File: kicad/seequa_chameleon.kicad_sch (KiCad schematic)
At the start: 0 parts

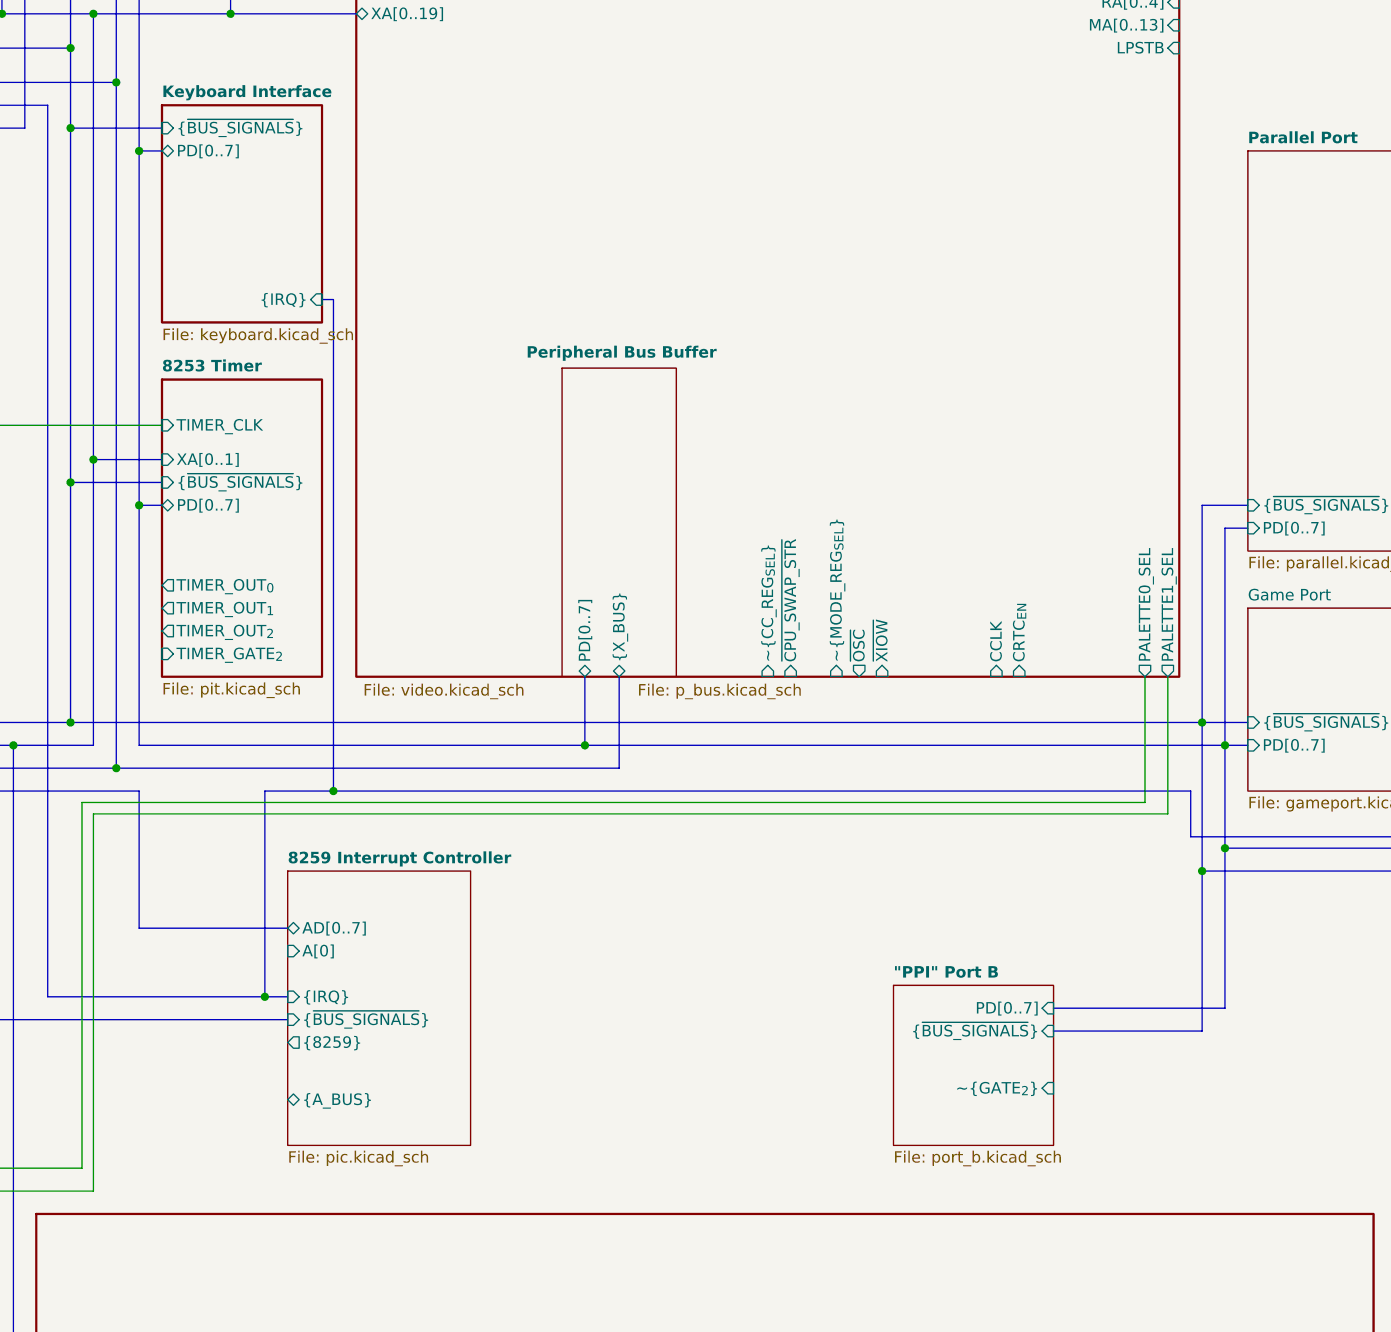
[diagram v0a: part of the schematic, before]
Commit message: Fixes to clocks,  keyboard controller stuff.
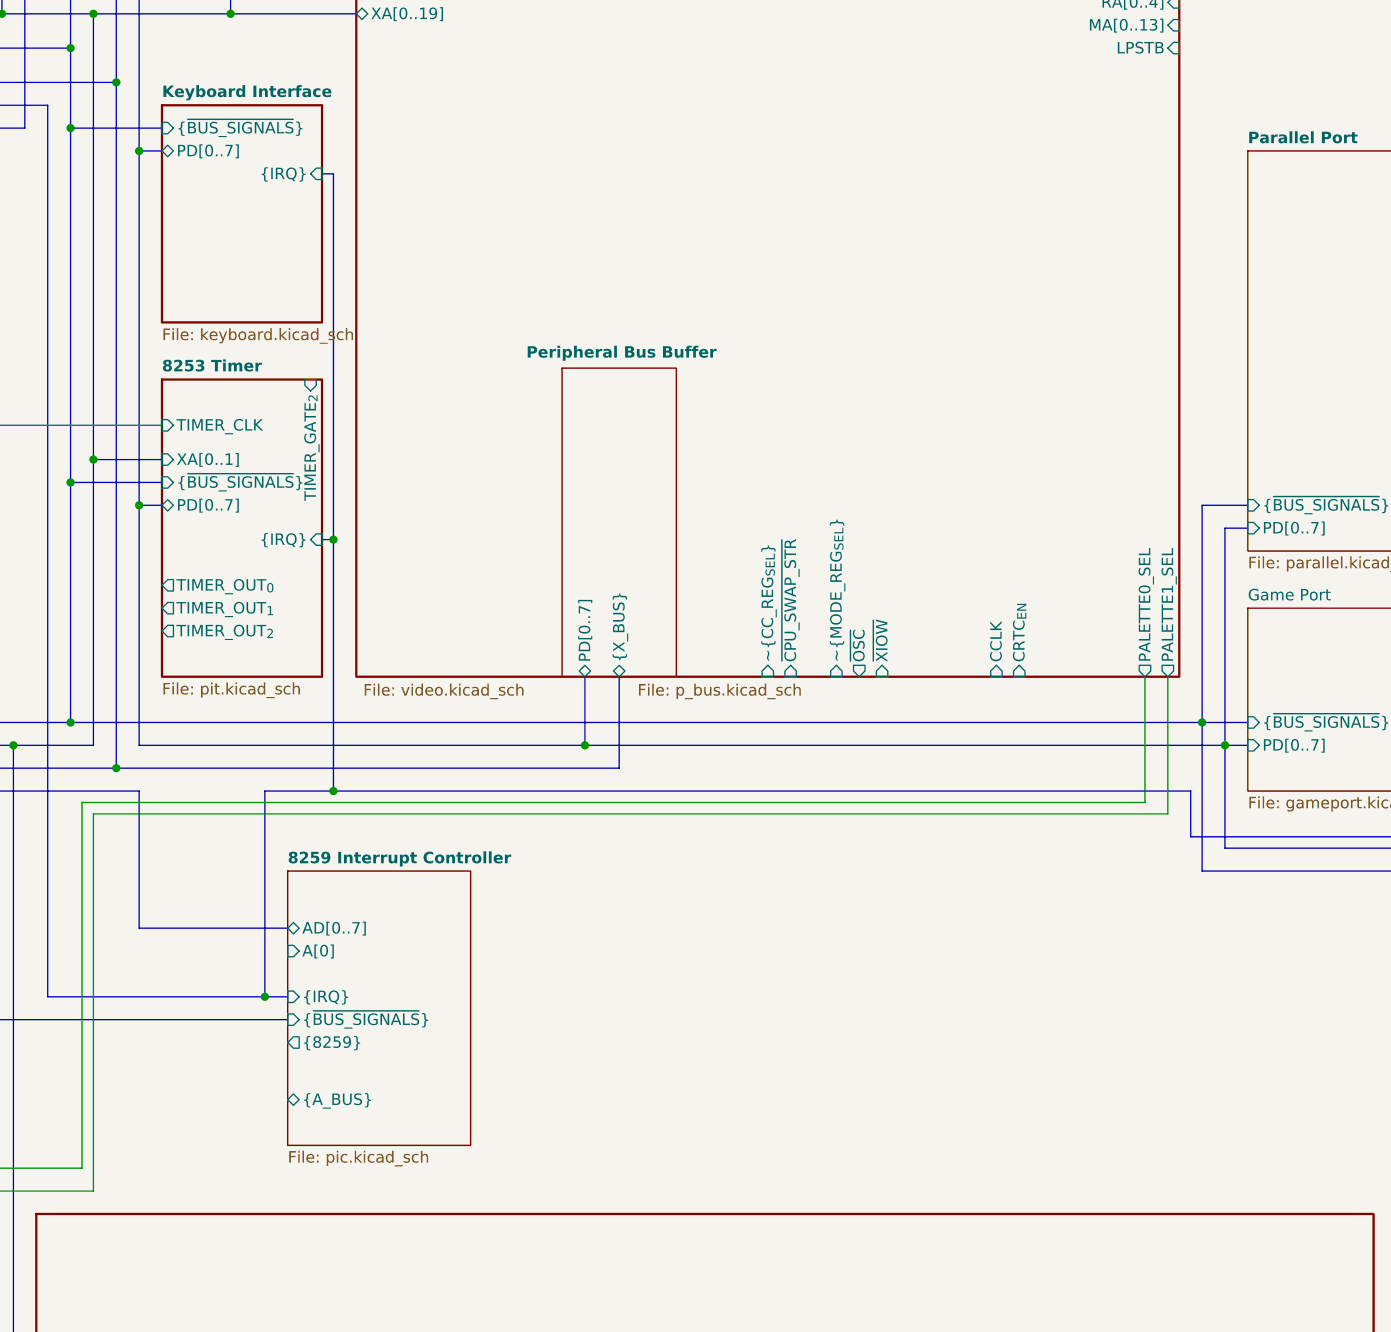
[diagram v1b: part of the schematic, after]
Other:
- removed sheet "PPI" Port B
- sheet 8253 Timer ports: added {IRQ}; removed none
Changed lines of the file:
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@@
 	)
 	(junction
-		(at 267.97 171.45)
-		(diameter 0)
-		(color 0 0 0 0)
-	)
-	(junction
 		(at 199.39 157.48)
 		(diameter 0)
@@
 	)
 	(junction
-		(at 270.51 168.91)
+		(at 171.45 134.62)
 		(diameter 0)
 		(color 0 0 0 0)
@@
 	(bus
 		(pts
-			(xy 170.18 107.95) (xy 171.45 107.95)
+			(xy 170.18 93.98) (xy 171.45 93.98)
 		)
 		(stroke
@@
 	(bus
 		(pts
-			(xy 270.51 168.91) (xy 270.51 186.69)
-		)
-		(stroke
-			(width 1)
-			(type default)
-			(color 0 132 0 1)
-		)
-	)
-	(bus
-		(pts
 			(xy 110.49 199.39) (xy 110.49 201.93)
 		)
@@
 	(bus
 		(pts
-			(xy 251.46 189.23) (xy 267.97 189.23)
+			(xy 162.56 71.12) (xy 173.99 71.12)
 		)
 		(stroke
@@
 	(bus
 		(pts
-			(xy 162.56 71.12) (xy 173.99 71.12)
+			(xy 266.7 167.64) (xy 293.37 167.64)
 		)
 		(stroke
-			(width 1)
+			(width 0)
 			(type default)
-			(color 194 194 0 1)
 		)
 	)
 	(bus
 		(pts
-			(xy 266.7 167.64) (xy 293.37 167.64)
+			(xy 270.51 157.48) (xy 273.05 157.48)
 		)
 		(stroke
-			(width 0)
+			(width 1)
 			(type default)
+			(color 0 132 0 1)
 		)
 	)
 	(bus
 		(pts
-			(xy 270.51 157.48) (xy 273.05 157.48)
+			(xy 170.18 134.62) (xy 171.45 134.62)
 		)
 		(stroke
-			(width 1)
+			(width 0)
 			(type default)
-			(color 0 132 0 1)
 		)
 	)
@@
 	(bus
 		(pts
-			(xy 171.45 107.95) (xy 171.45 162.56)
+			(xy 171.45 93.98) (xy 171.45 134.62)
 		)
 		(stroke
@@
 	(bus
 		(pts
-			(xy 270.51 186.69) (xy 251.46 186.69)
+			(xy 144.78 125.73) (xy 144.78 157.48)
 		)
 		(stroke
 			(width 1)
 			(type default)
-			(color 0 132 0 1)
+			(color 204 102 0 1)
 		)
 	)
 	(bus
 		(pts
-			(xy 144.78 125.73) (xy 144.78 157.48)
+			(xy 171.45 134.62) (xy 171.45 162.56)
 		)
 		(stroke
-			(width 1)
+			(width 0)
 			(type default)
-			(color 204 102 0 1)
 		)
 	)
@@
 	(bus
 		(pts
-			(xy 267.97 171.45) (xy 267.97 189.23)
-		)
-		(stroke
-			(width 1)
-			(type default)
-			(color 194 194 0 1)
-		)
-	)
-	(bus
-		(pts
 			(xy 121.92 68.58) (xy 121.92 69.85)
 		)
@@
 		)
 		(pin "TIMER_GATE_{2}" input
-			(at 152.4 147.32 180)
+			(at 168.91 116.84 90)
 			(effects
 				(font
 					(size 1.27 1.27)
 				)
-				(justify left)
+				(justify right)
 			)
 		)
@@
 			)
 		)
+		(pin "{IRQ}" input
+			(at 170.18 134.62 0)
+			(effects
+				(font
+					(size 1.27 1.27)
+				)
+				(justify right)
+			)
+		)
 		(instances
 			(project "seequa_chameleon"
@@
 		)
 		(pin "{IRQ}" input
-			(at 170.18 107.95 0)
+			(at 170.18 93.98 0)
 			(effects
 				(font
@@
 				)
 			)
-		)
-	)
-	(sheet
-		(at 233.68 184.15)
-		(size 17.78 17.78)
-		(exclude_from_sim no)
-		(in_bom yes)
-		(on_board yes)
-		(dnp no)
-		(fields_autoplaced yes)
-		(stroke
-			(width 0.1524)
-			(type solid)
-		)
-		(fill
-			(color 0 0 0 0.0000)
-		)
-		(property "Sheetname" "\"PPI\" Port B"
-			(at 233.68 183.4384 0)
-			(effects
-				(font
-					(size 1.27 1.27)
-					(thickness 0.254)
-					(bold yes)
-				)
-				(justify left bottom)
-			)
-		)
-		(property "Sheetfile" "port_b.kicad_sch"
-			(at 233.68 202.5146 0)
-			(effects
-				(font
-					(size 1.27 1.27)
-				)
-				(justify left top)
-			)
-		)
-		(pin "PD[0..7]" input
-			(at 251.46 186.69 0)
-			(effects
-				(font
-					(size 1.27 1.27)
-				)
-				(justify right)
-			)
-		)
-		(pin "{~{BUS_SIGNALS}}" input
-			(at 251.46 189.23 0)
-			(effects
-				(font
-					(size 1.27 1.27)
-				)
-				(justify right)
-			)
-		)
-		(pin "~{GATE_{2}}" input
-			(at 251.46 195.58 0)
-			(effects
-				(font
-					(size 1.27 1.27)
-				)
-				(justify right)
-			)
-		)
-		(instances
-			(project "seequa_chameleon"
-				(path "/ae890d4c-6a02-4621-80ce-7ef4317218ea"
-					(page "27")
-				)
-			)

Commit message: update kicad project
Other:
- sheet Data Entry renamed Power, Ground and Filtering
- sheet IO Decoder renamed IO Address Decoders
- sheet Keyboard Interface renamed Keyboard PAL
- sheet Logic Unit renamed CPU Logic Unit
- sheet Speaker renamed Speaker Connector
- sheet 8237 DMA Controller ports: added {~{BUS_SIGNALS}}, ~{IOS_TO_DCON}; removed ADSTB, ~{DMA_{CS}}
- sheet 8253 Timer ports: added XA[0..19], {X_BUS}; removed TIMER_GATE_{2}, TIMER_OUT_{0}, TIMER_OUT_{1}, TIMER_OUT_{2}, XA[0..1]
- sheet 8259 Interrupt Controller ports: added {X_BUS}; removed A[0], {8259}, {A_BUS}
- sheet 8274 Serial Controller ports: added PD[0..7]; removed none
- sheet CPU Logic Unit ports: added {DMA}, {IRQ}, ~{SP}/~{EN}; removed ALE, MEMR, S[0..2], ~{8259_{CS}}, ~{INTA}
- sheet Floppy Controller ports: added PD[0..7], {DMA}, {X_BUS}; removed XD[0..7]
- sheet GPIB Interface ports: added PD[0..7], {X_BUS}; removed none
- sheet Game Port ports: added ~{GAMEPORT_{RD}}, ~{GAMEPORT_{WR}}; removed none
- sheet IO Address Decoders ports: added ~{GAMEPORT_{RD}}, ~{GAMEPORT_{WR}}, ~{IOS_TO_DCON}; removed none
- sheet Keyboard PAL ports: added SPEAKER_OUT, {X_BUS}; removed none
- sheet Parallel Port ports: added {X_BUS}; removed none
- sheet Power, Ground and Filtering ports: added none; removed IRQ1, XA[0..19]
- sheet RAM ports: added {MA[0..7],~{RAS_{[0..3]}}}; removed MA[0..7], MUX_SEL, ~{ROM_SEL}
- sheet ROM and NOVRAM ports: added ~{PALETTE0_{WR}}, ~{PALETTE1_{WR}}; removed D[0..7], MRDC, PALETTE0_SEL, PALETTE1_SEL, ~{ROM_SEL}
- sheet Video Unit ports: added ~{PALETTE0_{WR}}, ~{PALETTE1_{WR}}; removed LPSTB, MA[0..13], OSC, PALETTE0_SEL, PALETTE1_SEL, RA[0..4], VD[0..7], ~{CC_REG_{SEL}}, ~{CPU_SWAP_STR}, ~{MODE_REG_{SEL}}, ~{OSC}, ~{RESET}, ~{XIOW}

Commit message: More updates
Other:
- sheet RAM ports: added {DMA}, {RR_BUS}; removed A[0..7], MD[0..8], {MA[0..7],~{RAS_{[0..3]}}}, ~{WR}
- sheet ROM and NOVRAM ports: added {RR_BUS}; removed ~{WR}
- sheet Video Unit ports: added none; removed CCLK, CRTC_{EN}, FA[0..7]
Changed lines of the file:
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@@
 	)
 	(junction
-		(at 147.32 96.52)
+		(at 139.7 96.52)
 		(diameter 0)
 		(color 0 0 0 0)
@@
 	)
 	(junction
+		(at 147.32 93.98)
+		(diameter 0)
+		(color 0 0 0 0)
+	)
+	(junction
 		(at 142.24 88.9)
 		(diameter 0)
@@
 	)
 	(junction
+		(at 133.35 222.25)
+		(diameter 0)
+		(color 0 0 0 0)
+	)
+	(junction
 		(at 139.7 162.56)
 		(diameter 0)
@@
 	)
 	(junction
-		(at 139.7 93.98)
-		(diameter 0)
-		(color 0 0 0 0)
-	)
-	(junction
 		(at 147.32 82.55)
 		(diameter 0)
@@
 	(bus
 		(pts
-			(xy 147.32 96.52) (xy 152.4 96.52)
+			(xy 147.32 93.98) (xy 152.4 93.98)
 		)
 		(stroke
@@
 		)
 	)
+	(bus
+		(pts
+			(xy 133.35 222.25) (xy 133.35 269.24)
+		)
+		(stroke
+			(width 0.75)
+			(type default)
+			(color 132 0 132 1)
+		)
+	)
 	(wire
 		(pts
@@
 		)
 	)
-	(wire
-		(pts
-			(xy 128.27 242.57) (xy 138.43 242.57)
-		)
-		(stroke
-			(width 0)
-			(type default)
-		)
-	)
 	(bus
 		(pts
@@
 	(bus
 		(pts
-			(xy 139.7 93.98) (xy 152.4 93.98)
+			(xy 139.7 96.52) (xy 152.4 96.52)
 		)
 		(stroke
@@
 	(bus
 		(pts
-			(xy 147.32 96.52) (xy 147.32 130.81)
+			(xy 147.32 82.55) (xy 147.32 93.98)
 		)
 		(stroke
@@
 	(bus
 		(pts
-			(xy 147.32 82.55) (xy 147.32 96.52)
-		)
-		(stroke
-			(width 0.75)
-			(type default)
-			(color 0 0 255 1)
-		)
-	)
-	(bus
-		(pts
 			(xy 128.27 77.47) (xy 144.78 77.47)
 		)
@@
 	(bus
 		(pts
-			(xy 128.27 93.98) (xy 139.7 93.98)
+			(xy 128.27 96.52) (xy 139.7 96.52)
 		)
 		(stroke
@@
 		)
 	)
-	(wire
-		(pts
-			(xy 232.41 149.86) (xy 237.49 149.86)
-		)
-		(stroke
-			(width 0)
-			(type default)
-		)
-	)
 	(bus
 		(pts
@@
 	(bus
 		(pts
+			(xy 139.7 96.52) (xy 139.7 135.89)
+		)
+		(stroke
+			(width 0)
+			(type default)
+		)
+	)
+	(bus
+		(pts
 			(xy 135.89 227.33) (xy 135.89 274.32)
 		)
@@
 		)
 	)
+	(bus
+		(pts
+			(xy 133.35 222.25) (xy 138.43 222.25)
+		)
+		(stroke
+			(width 0.75)
+			(type default)
+			(color 132 0 132 1)
+		)
+	)
+	(bus
+		(pts
+			(xy 147.32 93.98) (xy 147.32 130.81)
+		)
+		(stroke
+			(width 0.75)
+			(type default)
+			(color 0 0 255 1)
+		)
+	)
 	(wire
 		(pts
@@
 	(bus
 		(pts
-			(xy 133.35 161.29) (xy 133.35 269.24)
+			(xy 133.35 161.29) (xy 133.35 222.25)
 		)
 		(stroke
@@
 		)
 	)
-	(wire
-		(pts
-			(xy 128.27 219.71) (xy 138.43 219.71)
-		)
-		(stroke
-			(width 0)
-			(type default)
-		)
-	)
 	(bus
 		(pts
@@
 	(bus
 		(pts
-			(xy 139.7 93.98) (xy 139.7 135.89)
-		)
-		(stroke
-			(width 0)
-			(type default)
-		)
-	)
-	(bus
-		(pts
 			(xy 142.24 128.27) (xy 142.24 157.48)
 		)
@@
 			)
 		)
-		(pin "~{WR}" input
-			(at 128.27 242.57 0)
+		(pin "{X_BUS}" bidirectional
+			(at 128.27 224.79 0)
 			(effects
 				(font
@@
 			)
 		)
-		(pin "{X_BUS}" bidirectional
-			(at 128.27 224.79 0)
+		(pin "~{PALETTE0_{WR}}" output
+			(at 128.27 205.74 0)
 			(effects
 				(font
@@
 			)
 		)
-		(pin "~{PALETTE0_{WR}}" output
-			(at 128.27 205.74 0)
+		(pin "~{PALETTE1_{WR}}" output
+			(at 128.27 208.28 0)
 			(effects
 				(font
@@
 			)
 		)
-		(pin "~{PALETTE1_{WR}}" output
-			(at 128.27 208.28 0)
+		(pin "{RR_BUS}" bidirectional
+			(at 128.27 234.95 0)
 			(effects
 				(font
@@
 			)
 		)
-		(pin "A[0..7]" input
-			(at 138.43 237.49 180)
-			(effects
-				(font
-					(size 1.27 1.27)
-				)
-				(justify left)
-			)
-		)
-		(pin "MD[0..8]" bidirectional
-			(at 138.43 240.03 180)
-			(effects
-				(font
-					(size 1.27 1.27)
-				)
-				(justify left)
-			)
-		)
-		(pin "~{WR}" input
-			(at 138.43 242.57 180)
+		(pin "{DMA}" input
+			(at 138.43 222.25 180)
 			(effects
 				(font
@@
 			)
 		)
-		(pin "{MA[0..7],~{RAS_{[0..3]}}}" bidirectional
-			(at 138.43 222.25 180)
+		(pin "{RR_BUS}" bidirectional
+			(at 138.43 234.95 180)
 			(effects
 				(font
@@
 		)
 		(pin "{IRQ}" input
-			(at 152.4 93.98 180)
+			(at 152.4 96.52 180)
 			(effects
 				(font
@@
 		)
 		(pin "{X_BUS}" input
-			(at 152.4 96.52 180)
+			(at 152.4 93.98 180)
 			(effects
 				(font
@@
 		)
 		(pin "{IRQ}" input
-			(at 128.27 93.98 0)
+			(at 128.27 96.52 0)
 			(effects
 				(font
@@
 			)
 		)
-		(pin "CCLK" input
-			(at 245.11 149.86 270)
-			(effects
-				(font
-					(size 1.27 1.27)
-				)
-				(justify left)
-			)
-		)
-		(pin "CRTC_{EN}" input
-			(at 247.65 149.86 270)
-			(effects
-				(font
-					(size 1.27 1.27)
-				)
-				(justify left)
-			)
-		)
-		(pin "FA[0..7]" input
-			(at 237.49 149.86 270)
-			(effects
-				(font
-					(size 1.27 1.27)
-				)
-				(justify left)
-			)
-		)

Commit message: Add parallel port, game port
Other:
- sheet 8274 Serial Controller ports: added {DMA}; removed none
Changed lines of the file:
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@@
 	)
 	(junction
+		(at 298.45 170.18)
+		(diameter 0)
+		(color 0 0 0 0)
+	)
+	(junction
 		(at 203.2 160.02)
 		(diameter 0)
@@
 	(bus
 		(pts
+			(xy 298.45 170.18) (xy 347.98 170.18)
+		)
+		(stroke
+			(width 0.75)
+			(type default)
+			(color 132 0 132 1)
+		)
+	)
+	(bus
+		(pts
 			(xy 128.27 234.95) (xy 138.43 234.95)
 		)
@@
 	(bus
 		(pts
-			(xy 266.7 170.18) (xy 347.98 170.18)
+			(xy 266.7 170.18) (xy 298.45 170.18)
 		)
 		(stroke
@@
 	(bus
 		(pts
+			(xy 298.45 170.18) (xy 298.45 172.72)
+		)
+		(stroke
+			(width 0.75)
+			(type default)
+			(color 132 0 132 1)
+		)
+	)
+	(bus
+		(pts
 			(xy 139.7 162.56) (xy 270.51 162.56)
 		)
@@
 			(effects
 				(font
+					(size 1.27 1.27)
+				)
+				(justify right)
+			)
+		)
+		(pin "{DMA}" input
+			(at 298.45 172.72 90)
+			(effects
+				(font
